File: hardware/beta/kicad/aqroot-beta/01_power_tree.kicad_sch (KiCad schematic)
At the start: 53 parts, among them J3 USB_C_Receptacle_USB2.0_16P, J4 JST-PH-2 BATTERY, SW9 SW_SPST, U10 USBLC6-2SC6, U11 BQ25185, U12 TPS63020, U13 TPS61023, U14 MAX17048

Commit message: AQROOT Beta: lock mechanical component selections
Records exact MPN / manufacturer / package metadata for the mechanical
parts. All four footprints stay BLANK - every one needs a vendor drawing.

  SW9  JS102011SAQN     C&K (Littelfuse)      right-angle SMD SPDT slide
  J2   5025700893       Molex                 SMT push-push microSD, 8 contacts
  LS1  CMS-1535-058SP   Same Sky (CUI)        15 mm round 8 ohm solder-pad
  J1   Adafruit 2770    Adafruit              2.8in 240x320 + FT6236U cap touch

SW9 - SYMBOL/PART CONFLICT FOUND, NOT PAPERED OVER:
JS102011SAQN is a 3-terminal SPDT, but this instance uses Switch:SW_SPST
which has only two pins (A,B). Any correct land pattern for this part has
three signal pads plus mounting tabs, so symbol and footprint cannot agree
as they stand. The locked electrical intent is SPST (VINA -> switch -> EN,
never switching GND) and wiring an SPDT as SPST is fine, but the symbol has
to expose the unused throw so it can carry a no-connect. Swapping the symbol
is an approval-gated change and was deliberately NOT made. Recorded in the
part's Note so it cannot be missed at footprint time.

J1 is recorded as a VENDOR SKU lock, not a production MPN lock - Adafruit
can change panel manufacturer while preserving compatibility. Its Note
marks it a critical PCB/enclosure dependency and lists what is still needed:
the current Adafruit mechanical/FPC drawing, verification of the 50-pin
0.5 mm FPC pinout against the existing sheet architecture, and selection of
the separate mating FPC connector. The ~69 x 50 x 4 mm figure is flagged
approximate.

SW1-SW8 were deliberately left without MPNs. The class is locked (compact
SMD tactile) but the enclosure doc specifies only that there are seven
controls - D-pad, A and B - with no top-push versus side-push actuation
requirement recorded, so no per-reference MPN could be justified without
inventing a mechanical decision.

No fabricated dimensions, land patterns or ratings. Electrical circuits,
signal ar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
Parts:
- SW9: MPN (none) -> JS102011SAQN; Manufacturer (none) -> C&K (Littelfuse); Note (none) -> SYMBOL/PART CONFLICT - MUST BE RESOLVED BEFORE FOOTPRINT. J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; Package (none) -> Right-angle SMD SPDT slide switch - part LOCKED. Footprint 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
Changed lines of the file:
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@@
+			)
+		)
+		(property "Note" "SYMBOL/PART CONFLICT - MUST BE RESOLVED BEFORE FOOTPRINT. JS102011SAQN is a 3-terminal SPDT; this instance uses Switch:SW_SPST which has only 2 pins (A,B). Any correct JS102011SAQN land pattern has 3 signal pads plus mounting tabs, so symbol and footprint cannot agree as-is. The locked electrical intent is SPST (VINA -> switch -> EN, never switching GND); wiring an SPDT as SPST is fine, but the symbol must then expose the unused throw so it can carry a no-connect. Changing the symbol is an approval-gated change and was NOT made here. Actuator direction and travel also still require the enclosure mechanical review."
+			(at 190.5 63.5 0)
+			(hide yes)
+			(show_name no)
+			(do_not_autoplace no)
+			(effects
+				(font
+					(size 1.27 1.27)
+				)
+			)
+		)
+		(property "Package" "Right-angle SMD SPDT slide switch - part LOCKED. Footprint BLOCKED: needs the official C&K PCB layout drawing, and see the SYMBOL CONFLICT below."
+			(at 190.5 63.5 0)
+			(hide yes)
+			(show_name no)
+			(do_not_autoplace no)
+			(effects
+				(font
+					(size 1.27 1.27)
+				)
+			)
+		)
+		(property "Manufacturer" "C&K (Littelfuse)"
+			(at 190.5 63.5 0)
+			(hide yes)
+			(show_name no)
+			(do_not_autoplace no)
+			(effects
+				(font
+					(size 1.27 1.27)
+				)
+			)
+		)
+		(property "MPN" "JS102011SAQN"
+			(at 190.5 63.5 0)
+			(hide yes)
+			(show_name no)
+			(do_not_autoplace no)
+			(effects
+				(font
+					(size 1.27 1.27)
+				)
 			)
 		)

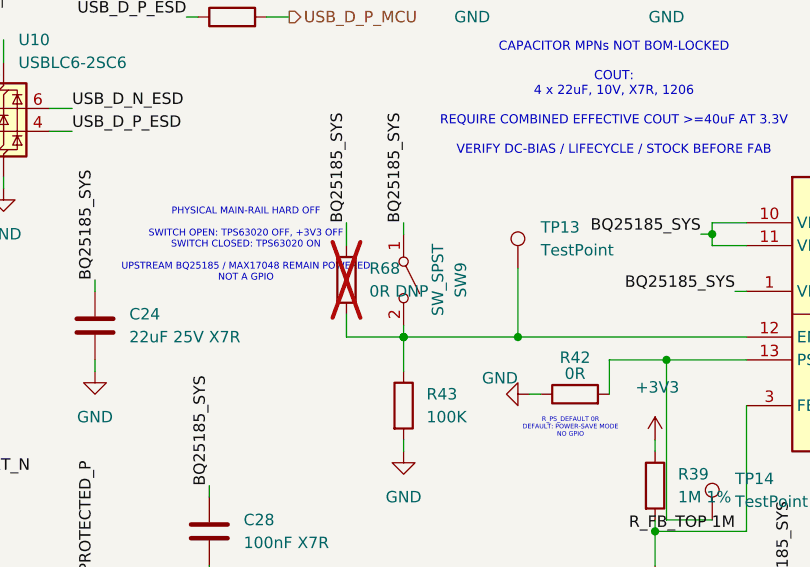
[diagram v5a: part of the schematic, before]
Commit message: AQROOT Beta: match hard-off switch to JS102011SAQN
The locked C&K JS102011SAQN is a 3-terminal SPDT; SW9 used the 2-pin
Switch:SW_SPST, which no correct land pattern could match. C&K JS-series
documentation confirms terminal 2 = C = common/pole, so the symbol is now
SPDT with all three physical terminals exposed.

  terminal 2  common      -> /01_POWER_TREE/BQ25185_SYS   (symbol pin 2)
  terminal 1  used throw  -> EN net -> U12.12             (symbol pin 1)
  terminal 3  unused throw-> explicit no-connect          (symbol pin 3)

SW9 stays at (190.5, 63.5) rot 270, so common lands exactly on the existing
BQ25185_SYS wire endpoint (190.5, 58.42) with no rewiring on that side. Added
one 2.54 mm wire (193.04,68.58)->(190.5,68.58) joining the used throw to the
existing EN wire, and a no_connect at (187.96,68.58) on the unused throw. All
coordinates on the 1.27 mm grid. Switch:SW_SPDT added to the sheet's
lib_symbols cache in alphabetical position.

Electrical behaviour unchanged. The EN net keeps exactly its previous members
- R43.1, R68.2, TP13.1, U12.12 - with SW9 contributing one terminal as before.
KiCad's auto-generated name for that unnamed net changes Net-(SW9-B) ->
Net-(SW9-A) because the switch's contributing pin renumbers from 2 to 1; that
is a name change, not a membership change. R43 100k pull-down unchanged, R68
0R still dnp=yes spanning SYS<->EN, TP13 unchanged. No second functional
switch position is created - terminal 3 goes nowhere.

FOOTPRINT NOT ASSIGNED. Button_Switch_SMD:SW_SPDT_CK_JS102011SAQN is the
correct candidate and cites C&K's JS datasheet, but SW9 is Class B
(mechanical/placement-critical) and the C&K recommended PCB layout could not
be retrieved - ckswitches.com redirects to littelfuse.com, which returns HTTP
403. SW9 footprint remains BLOCKED_EXTERNAL_DOCUMENT.

Verified with kicad-cli: all sheets plot; ERC raw 48 / unique 24 / excluded 24
/ real 0; the unused throw's NC prevents a new pin_not_connected.

Co-Authored-By: Claude Opus 5 <no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
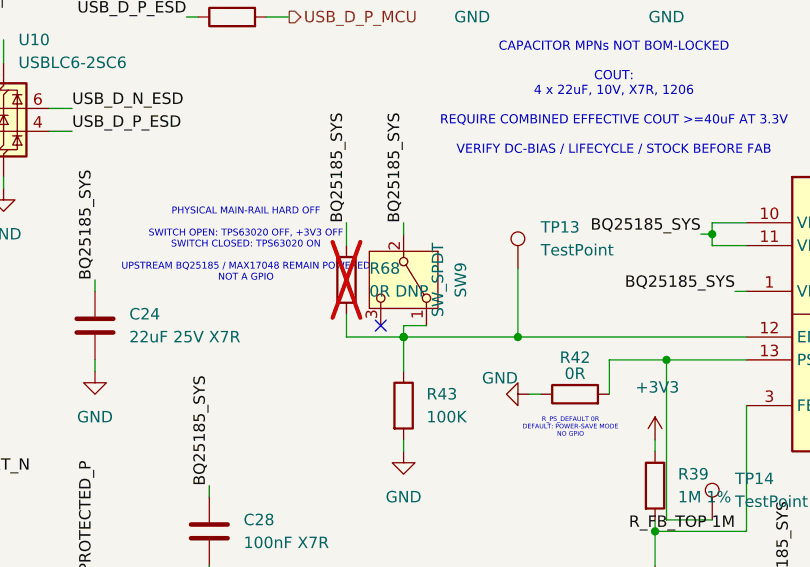
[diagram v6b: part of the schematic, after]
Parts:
- SW9: value SW_SPST -> SW_SPDT; symbol Switch:SW_SPST -> Switch:SW_SPDT
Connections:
- net BQ25185_SYS: now also SW9.2 (B); no longer SW9.1 (A)
- net at R43.1, R68.2, TP13.1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: now also SW9.1 (A); no longer SW9.2 (B)
- no-connect marks 3 -> 4
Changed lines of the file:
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@@
 	)
 	(no_connect
+		(at 187.96 68.58)
+	)
+	(no_connect
 		(at 45.72 62.23)
 	)
@@
 	(wire
 		(pts
+			(xy 193.04 68.58) (xy 190.5 68.58)
+		)
+		(stroke
+			(width 0)
+			(type default)
+		)
+	)
+	(wire
+		(pts
 			(xy 184.15 59.69) (xy 184.15 57.15)
 		)
@@
 	)
 	(symbol
-		(lib_id "Switch:SW_SPST")
+		(lib_id "Switch:SW_SPDT")
 		(at 190.5 63.5 270)
 		(unit 1)
@@
 			)
 		)
-		(property "Value" "SW_SPST"
+		(property "Value" "SW_SPDT"
 			(at 194.31 63.5 0)
 			(show_name no)
@@
 		(pin "2"
 		)
+		(pin "3"
+		)
 		(instances

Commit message: AQROOT Beta: record L1/L2 datasheet specifications; U12 package data confirmed absent
Second vendor-verification pass. No footprint was created or assigned - two
new blocks are now confirmed rather than assumed, and two placeholders are
closed with real datasheet values.

L1/L2 electrical and body data extracted from the manufacturer datasheets
and written into the schematic Notes, replacing the earlier 'take from the
datasheet, do not record from memory' placeholders:

  L1 XFL4020-152MEC  1.5uH +/-20%, DCR 14.40/15.80 mOhm, Isat 4.1/4.4/4.6 A,
                     Irms 6.7/9.1 A, SRF 59 MHz, 4.0x4.0x2.10 max
                     (Coilcraft doc 745-1 rev 03/10/26)
  L2 74438357010     1uH +/-20%, RDC 11.6/13.5 mOhm, Isat 6.2/12.5 A,
                     IRP,40K 10.25 A, fres 59 MHz, 4.1x4.1x3.1 max

L2's ratings close the outstanding check that it be adequate for the TI
TPS61023 5V boost - 6.2 A saturation and 10.25 A rated are far above any NFC
PA draw.

BOTH FOOTPRINTS REMAIN BLOCKED, and deliberately so. Each recommended land
pattern prints as three bare numbers - Coilcraft 0.98/2.37/3.4, Wurth
1.39/3.35/3.7 - and text extraction does not recover which is the span. For
each, two pad-centre solutions are arithmetically valid, differing by about
half a millimetre on a 4 mm part. Guessing was refused; both are trivially
resolvable by eye from the drawing, or by using Wurth's own EDA asset.
Also recorded: both vendors mark the start-of-winding lead, so whichever
footprint is built must carry that orientation marker.

U12 TPS63020DSJR: the full 34-page TI datasheet was retrieved and searched.
It confirms VSON/DSJ/14 pins in the packaging tables but contains NO package
outline and NO land pattern - unlike every other TI datasheet checked in this
project, which carry both. TI publishes the DSJ drawing separately. Confirmed
BLOCKED_EXTERNAL_DOCUMENT; no generic VSON substitute.

Retrieval failures this pass: Molex J2 timeout, ST U10 timeout (third
attempt), ADI U5 conne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
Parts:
- L1: Note 1.5 uH +/-20%, LCSC C3033018. Isat/DCR/current rating NOT r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 -> Coilcraft doc 745-1 rev 03/10/26: 1.5 uH +/-20%; DCR 14.40 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
- L2: Note TPS61023 NFC 5V boost inductor (L_NFC_BOOST). Body size, DC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 -> Wurth datasheet for 74438357010 (WE-MAPI 4030): 1 uH +/-20%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
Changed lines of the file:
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@@
 			)
 		)
-		(property "Note" "TPS61023 NFC 5V boost inductor (L_NFC_BOOST). Body size, DCR, Isat and current rating NOT recorded here - take them from the Wurth datasheet. Current rating must still be checked against the TI TPS61023 5V design calculation."
+		(property "Note" "Wurth datasheet for 74438357010 (WE-MAPI 4030): 1 uH +/-20%; RDC 11.6 mOhm typ / 13.5 max; Isat 6.2 A (10% drop) / 12.5 A (30%); IRP,40K 10.25 A max; fres 59 MHz. Body 4.1 x 4.1 mm +/-0.2, height 3.1 mm max. Marked with start-of-winding. These ratings supersede the earlier 'take from datasheet' placeholder and satisfy the outstanding check that L2 be rated for the TI TPS61023 5V boost. FOOTPRINT STILL BLOCKED: recommended land pattern prints 1.39 / 3.35 / 3.7 mm but which is the span is not recoverable from text; prefer Wurth's own EDA/KiCad asset."
 			(at 133.35 153.67 0)
 			(hide yes)
@@
 			)
 		)
-		(property "Note" "1.5 uH +/-20%, LCSC C3033018. Isat/DCR/current rating NOT recorded here - take them from the Coilcraft datasheet at BOM lock rather than from memory."
+		(property "Note" "Coilcraft doc 745-1 rev 03/10/26: 1.5 uH +/-20%; DCR 14.40 mOhm typ / 15.80 max; SRF 59 MHz typ; Isat 4.1 A (10% drop) / 4.4 A (20%) / 4.6 A (30%); Irms 6.7 A (20K rise) / 9.1 A (40K). Body 4.0 x 4.0 mm +/-0.3, height 2.10 mm max, terminals 0.82 x 1.57 mm. LCSC C3033018. Coilcraft marks the start (short) lead - connect high dv/dt there for lowest EMI; the footprint must carry that orientation marker. FOOTPRINT STILL BLOCKED: the recommended land pattern prints 0.98 / 2.37 / 3.4 mm but text extraction does not reveal which dimension is the span, so pad centres cannot be fixed without reading the drawing."
 			(at 248.92 40.64 0)
 			(hide yes)

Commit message: Footprints: add verified power component land patterns
Creates and assigns vendor-exact land patterns for both power inductors. The
land-pattern ambiguity that blocked these last pass is resolved: the pages
were rasterized with PyMuPDF and the dimension leader lines read visually, so
which callout attaches to which geometry is now known rather than inferred.

NEW project-local footprints:

  AQROOT_Beta:Coilcraft_XFL4020
    Coilcraft doc 745-3 rev 03/10/26 'Recommended Land Pattern'
    pad 0.98 x 3.4 mm, 2.37 mm centre-to-centre
    body 4.0 x 4.0 mm, 2.10 mm max height
    silkscreen bar on +X marks terminal direction / start (short) lead -
    connect high dv/dt there for lowest EMI, per the drawing note

  AQROOT_Beta:Wurth_WE-MAPI_4030_74438357010
    74438357010 datasheet rev 003.001 (2024-02-27)
    span 3.35 outer-to-outer, 1.39 solder-resist gap, 3.7 pad length
      -> pad width (3.35-1.39)/2 = 0.98, centre-to-centre 3.35-0.98 = 2.37
    body 4.1 x 4.1 mm, 3.1 mm max height
    dot on -X marks Start of Winding
    'No vias and traces in restricted area' - the 1.39 mm inter-pad gap is
    that area and is outlined on Dwgs.User with a note

Both readings were checked for self-consistency before use: Coilcraft's
terminals are 0.82 wide at 3.25 typ outer span, giving ~2.43 terminal
centres against a 2.37 land spacing; and the two parts independently produce
the same 0.98 mm pad width and 2.37 mm spacing, as expected for two 4 mm-class
inductors.

Assigned to L1 and L2. Verified with kicad-cli: both footprints parse and
plot; readback confirms pad 0.98x3.4 / 0.98x3.7 at +/-1.185 as intended;
netlist pin-to-net mapping byte-identical; ERC raw 48 / unique 24 /
excluded 24 / real 0.

Status for both: VERIFIED_VENDOR_EXACT.

Co-Authored-By: Claude Opus 5 <noreply@anthropic.com>
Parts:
- L1: footprint (none) -> AQROOT_Beta:Coilcraft_XFL4020
- L2: footprint (none) -> AQROOT_Beta:Wurth_WE-MAPI_4030_74438357010
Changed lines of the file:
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@@
 			)
 		)
-		(property "Footprint" ""
+		(property "Footprint" "AQROOT_Beta:Wurth_WE-MAPI_4030_74438357010"
 			(at 133.35 153.67 0)
 			(hide yes)
@@
 			)
 		)
-		(property "Footprint" ""
+		(property "Footprint" "AQROOT_Beta:Coilcraft_XFL4020"
 			(at 248.92 40.64 0)
 			(hide yes)
